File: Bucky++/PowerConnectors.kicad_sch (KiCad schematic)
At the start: 16 parts, among them J1 XT60PW-M, J11 XT30AW-M, J12 XT30AW-M, J13 XT30AW-M, J14 XT30AW-M, J17 XT30UPB-F, J18 XT30UPB-F, J2 XT60PW-F, J3 XT30PW-F, J4 XT30PW-F, J5 XT30PW-F, J6 XT30PW-F, J7 XT30UPB-F, J8 XT30UPB-F

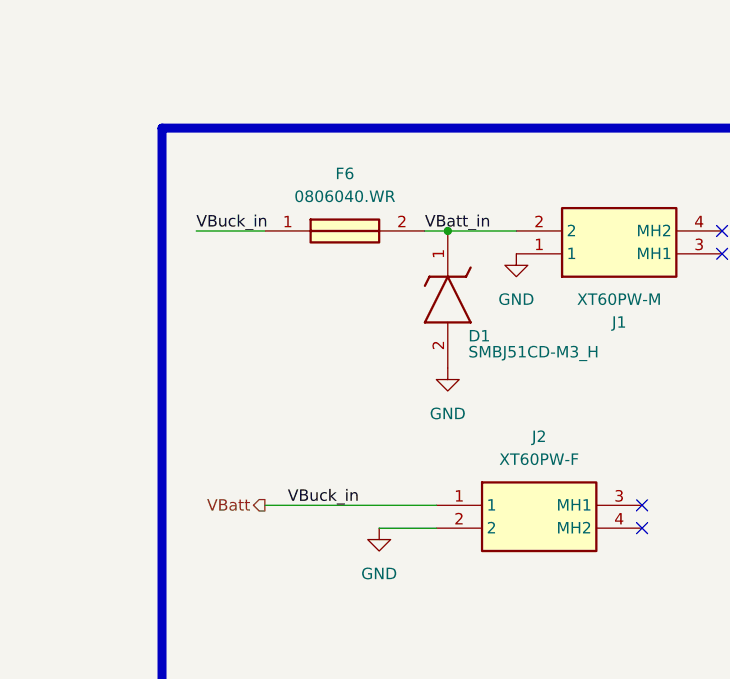
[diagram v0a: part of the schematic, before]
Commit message: added over-current protection on main input
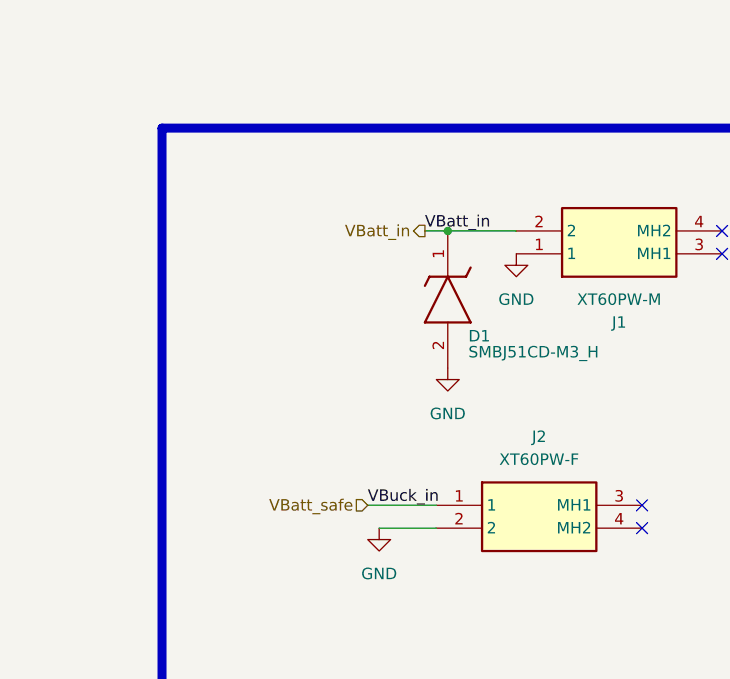
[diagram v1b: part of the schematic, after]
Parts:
- removed F6: 0806040.WR, SamacSys_Parts:FUSC3216X110N, symbol SamacSys_Parts:0806040.WR
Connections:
- net VBatt renamed VBatt_safe
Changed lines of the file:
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@@
 	(wire
 		(pts
-			(xy 36.83 50.8) (xy 44.45 50.8)
+			(xy 55.88 81.28) (xy 63.5 81.28)
 		)
 		(stroke
@@
 		(pts
 			(xy 110.49 92.71) (xy 118.11 92.71)
-		)
-		(stroke
-			(width 0)
-			(type default)
-		)
-	)
-	(wire
-		(pts
-			(xy 44.45 81.28) (xy 63.5 81.28)
 		)
 		(stroke
@@
 	)
 	(label "VBuck_in"
-		(at 36.83 50.8 0)
+		(at 55.88 81.28 0)
 		(effects
 			(font
@@
 	(label "Vout_12V"
 		(at 204.47 135.89 0)
-		(effects
-			(font
-				(size 1.27 1.27)
-			)
-			(justify left bottom)
-		)
-	)
-	(label "VBuck_in"
-		(at 46.99 81.28 0)
 		(effects
 			(font
@@
 		)
 	)
-	(hierarchical_label "VBatt"
+	(hierarchical_label "VBatt_safe"
+		(shape input)
+		(at 55.88 81.28 180)
+		(effects
+			(font
+				(size 1.27 1.27)
+			)
+			(justify right)
+		)
+	)
+	(hierarchical_label "VBatt_in"
 		(shape output)
-		(at 44.45 81.28 180)
+		(at 62.23 50.8 180)
 		(effects
 			(font
@@
 					(unit 1)
 				)
-			)
-		)
-	)
-	(symbol
-		(lib_id "SamacSys_Parts:0806040.WR")
-		(at 44.45 50.8 0)
-		(unit 1)
-		(exclude_from_sim no)
-		(in_bom yes)
-		(on_board yes)
-		(dnp no)
-		(fields_autoplaced yes)
-		(property "Reference" "F6"
-			(at 53.34 44.45 0)
-			(effects
-				(font
-					(size 1.27 1.27)
-				)
-			)
-		)
-		(property "Value" "0806040.WR"
-			(at 53.34 46.99 0)
-			(effects
-				(font
-					(size 1.27 1.27)
-				)
-			)
-		)
-		(property "Footprint" "SamacSys_Parts:FUSC3216X110N"
-			(at 58.42 146.99 0)
-			(effects
-				(font
-					(size 1.27 1.27)
-				)
-				(justify left top)
-				(hide yes)
-			)
-		)
-		(property "Datasheet" "https://www.littelfuse.com/assetdocs/littelfuse-fuse-806-datasheet?assetguid=a8479f54-3b43-4b97-8985-2bc550feee6f"
-			(at 58.42 246.99 0)
-			(effects
-				(font
-					(size 1.27 1.27)
-				)
-				(justify left top)
-				(hide yes)
-			)
-		)
-		(property "Description" "Surface Mount Fuses High Current 40A 36V , FUSE 36V HIGH CURRENT 1206 FA 40A | Series: 806 ,200A @ 36VDC"
-			(at 44.45 50.8 0)
-			(effects
-				(font
-					(size 1.27 1.27)
-				)
-				(hide yes)
-			)
-		)
-		(property "Height" "1.1"
-			(at 58.42 446.99 0)
-			(effects
-				(font
-					(size 1.27 1.27)
-				)
-				(justify left top)
-				(hide yes)
-			)
-		)
-		(property "Mouser Part Number" ""
-			(at 58.42 546.99 0)
-			(effects
-				(font
-					(size 1.27 1.27)
-				)
-				(justify left top)
-				(hide yes)
-			)
-		)
-		(property "Mouser Price/Stock" ""
-			(at 58.42 646.99 0)
-			(effects
-				(font
-					(size 1.27 1.27)
-				)
-				(justify left top)
-				(hide yes)
-			)
-		)
-		(property "Manufacturer_Name" "LITTELFUSE"
-			(at 58.42 746.99 0)
-			(effects
-				(font
-					(size 1.27 1.27)
-				)
-				(justify left top)
-				(hide yes)
-			)
-		)
-		(property "Manufacturer_Part_Number" "0806040.WR"
-			(at 58.42 846.99 0)
-			(effects
-				(font
-					(size 1.27 1.27)
-				)
-				(justify left top)
-				(hide yes)
-			)
-		)
-		(pin "2"
-		)
-		(pin "1"
-		)
-		(instances
-			(project "Bucky++"
-				(path "/0650c7a8-acba-429c-9f8e-eec0baf0bc1c/fede4c36-00cc-4d3d-b71c-5243ba232202/0b884d20-85c8-4e14-bcd5-df65213f1de9"
-					(reference "F6")
-					(unit 1)
-				)

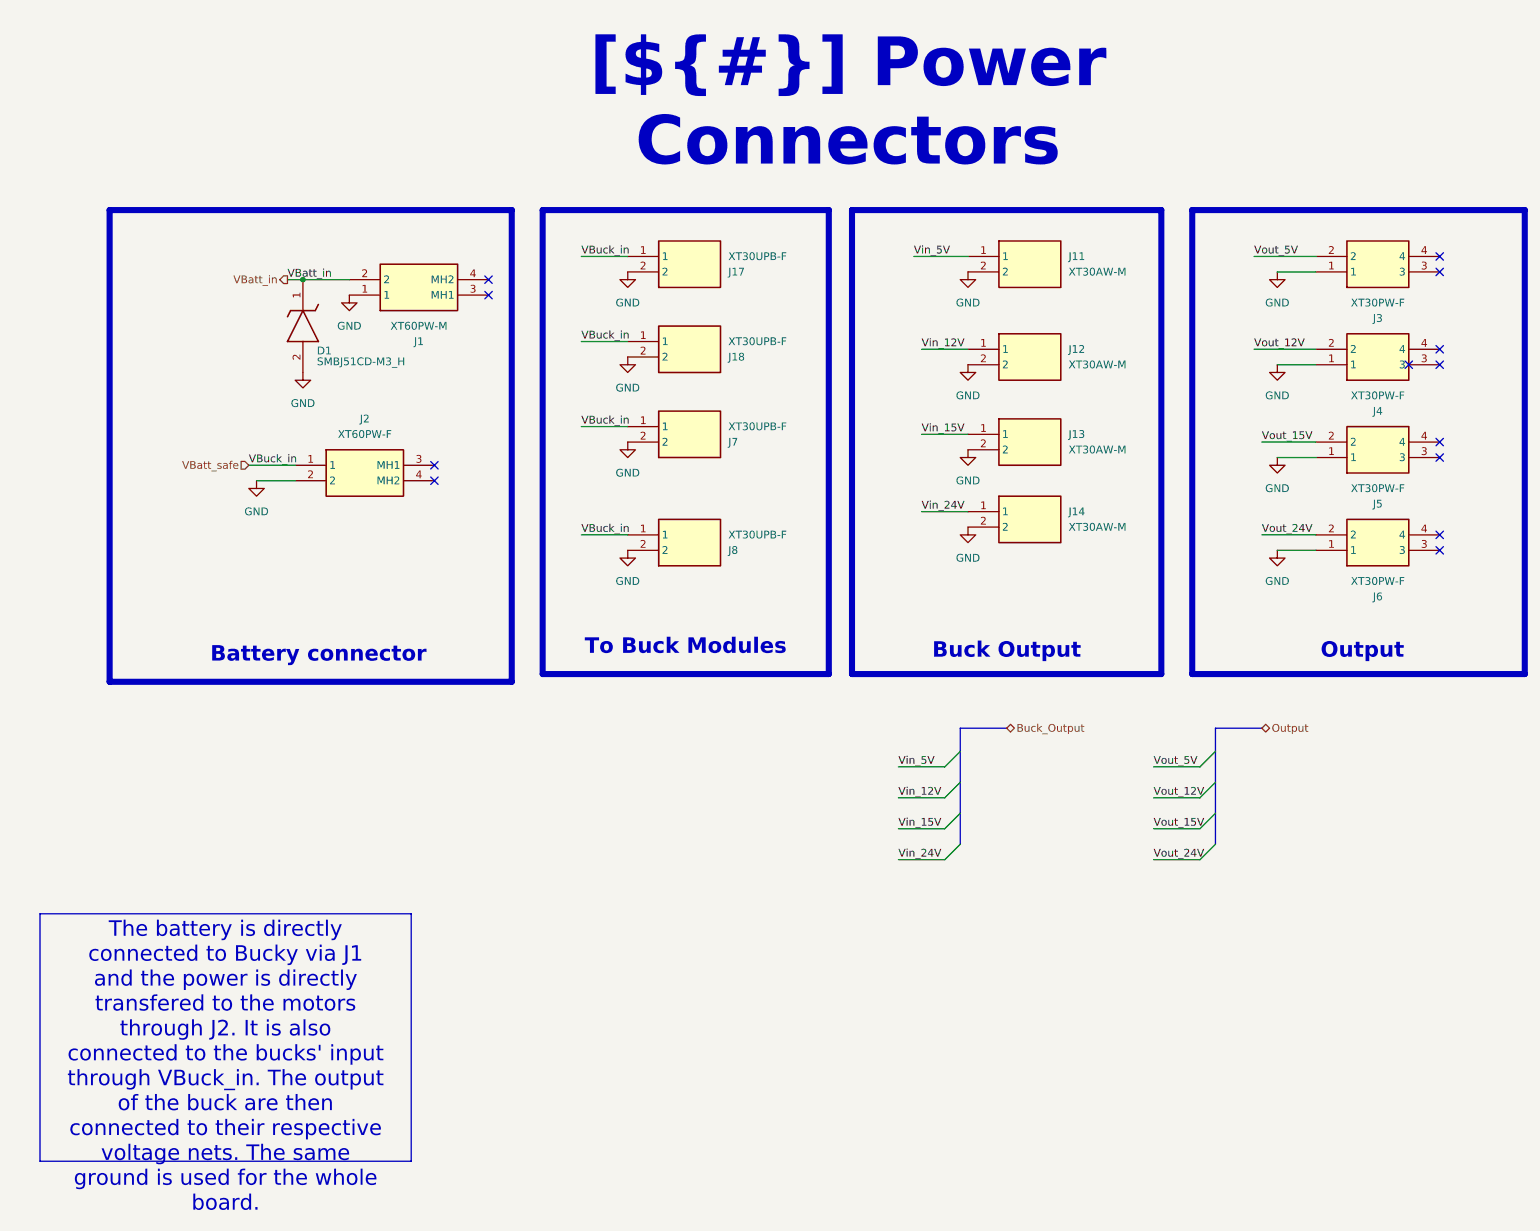
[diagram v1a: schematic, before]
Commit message: fixed errors and added protection diodes
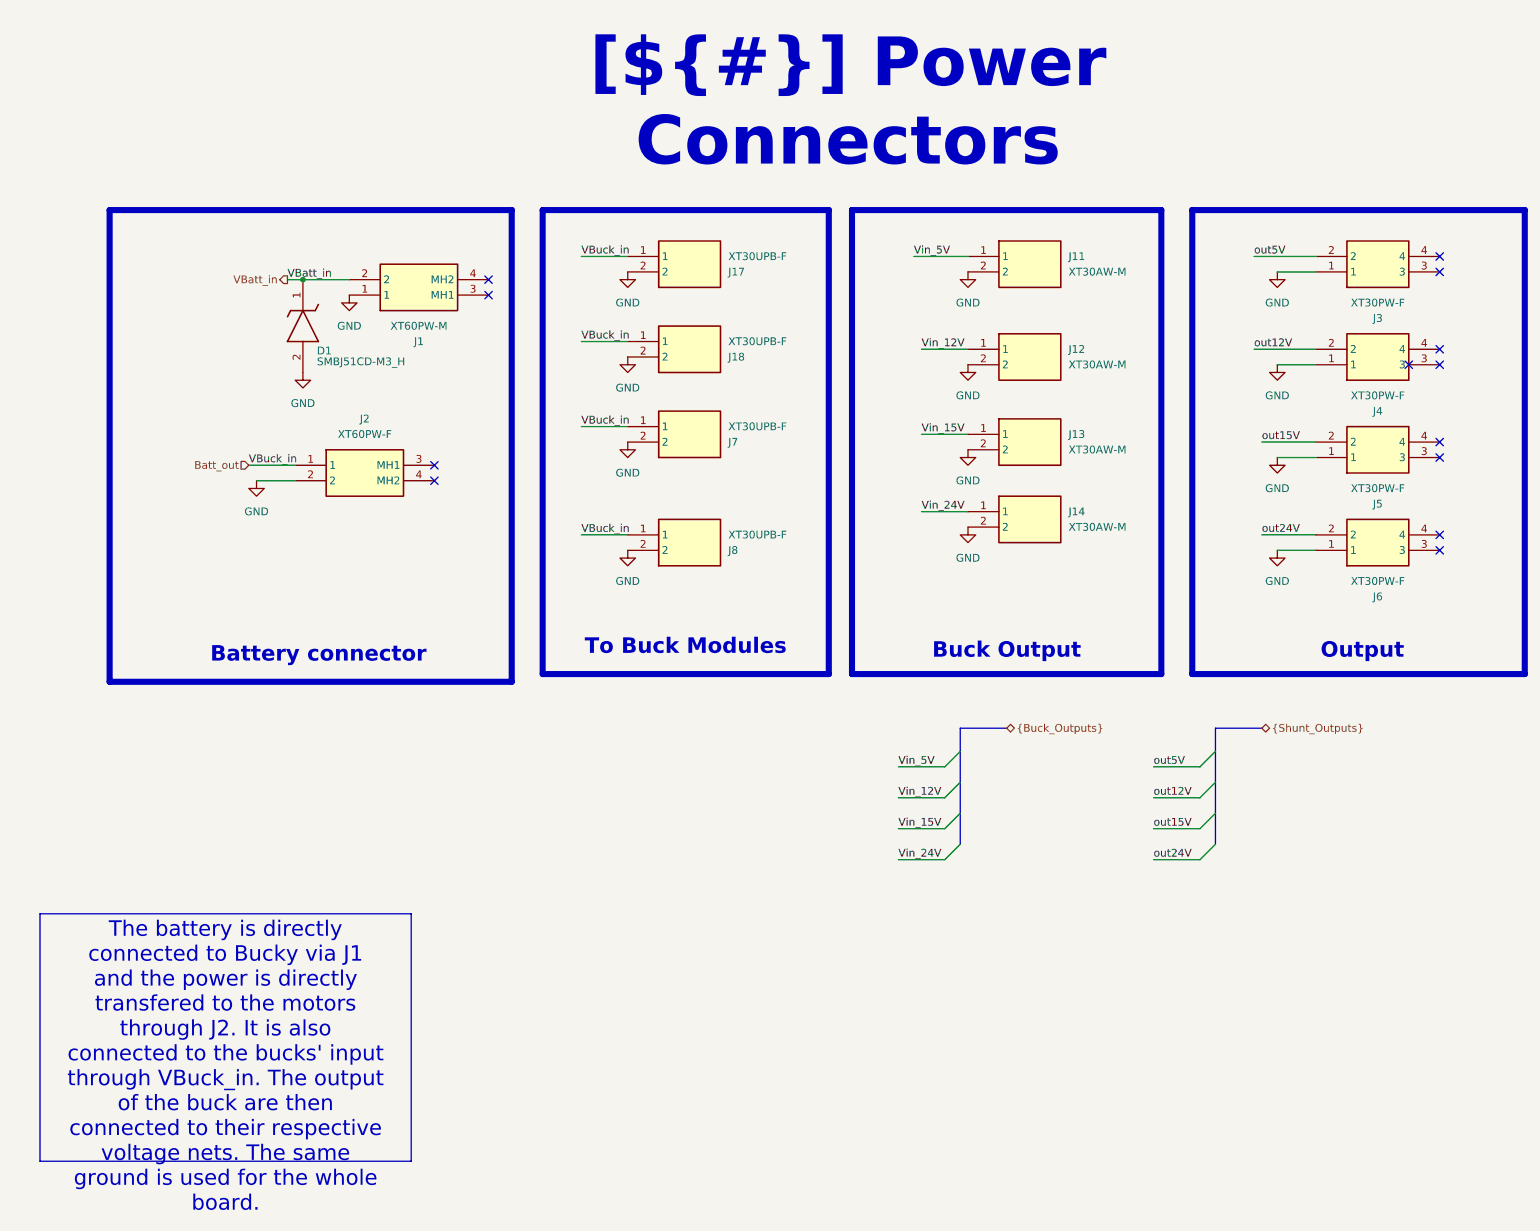
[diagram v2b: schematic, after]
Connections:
- net VBatt_safe renamed Batt_out
- net Vout_12V renamed out12V
- net Vout_15V renamed out15V
- net Vout_24V renamed out24V
- net Vout_5V renamed out5V
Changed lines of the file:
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@@
 		)
 	)
-	(label "Vout_5V"
+	(label "out5V"
 		(at 220.98 46.99 0)
 		(effects
@@
 		)
 	)
-	(label "Vout_24V"
+	(label "out24V"
 		(at 204.47 146.05 0)
 		(effects
@@
 		)
 	)
-	(label "Vout_24V"
+	(label "out24V"
 		(at 222.25 92.71 0)
 		(effects
@@
 		)
 	)
-	(label "Vout_15V"
+	(label "out15V"
 		(at 222.25 77.47 0)
 		(effects
@@
 		)
 	)
-	(label "Vout_12V"
+	(label "out12V"
 		(at 220.98 62.23 0)
 		(effects
@@
 		)
 	)
-	(label "Vout_5V"
+	(label "out5V"
 		(at 204.47 130.81 0)
 		(effects
@@
 		)
 	)
-	(label "Vout_12V"
+	(label "out12V"
 		(at 204.47 135.89 0)
 		(effects
@@
 		)
 	)
-	(label "Vout_15V"
+	(label "out15V"
 		(at 204.47 140.97 0)
 		(effects
@@
 		)
 	)
-	(hierarchical_label "Output"
+	(hierarchical_label "{Shunt_Outputs}"
 		(shape tri_state)
 		(at 222.25 124.46 0)
@@
 		)
 	)
-	(hierarchical_label "VBatt_safe"
+	(hierarchical_label "Batt_out"
 		(shape input)
 		(at 55.88 81.28 180)
@@
 		)
 	)
-	(hierarchical_label "Buck_Output"
+	(hierarchical_label "{Buck_Outputs}"
 		(shape tri_state)
 		(at 180.34 124.46 0)

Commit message: fixed issues after Pedro's review
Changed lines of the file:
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@@
 		)
 	)
-	(text_box "The battery is directly connected to Bucky via J1 and the power is directly transfered to the motors through J2. It is also connected to the bucks' input through VBuck_in. The output of the buck are then connected to their respective voltage nets. The same ground is used for the whole board.\n"
+	(text_box "DESIGN NOTE:\nThe battery is directly connected to Bucky via J1 and the power is directly transfered to the motors through J2. It is also connected to the bucks' input through VBuck_in. \nThe output of the buck are then connected to their respective voltage nets. \nThe same ground is used for the whole board.\n"
 		(exclude_from_sim no)
-		(at 21.59 154.94 0)
-		(size 60.96 40.64)
-		(margins 0.9525 0.9525 0.9525 0.9525)
+		(at 33.02 120.65 0)
+		(size 38.1 27.94)
+		(margins 1.3525 1.3525 1.3525 1.3525)
 		(stroke
-			(width 0.0508)
+			(width 0.8)
 			(type solid)
+			(color 200 200 200 1)
 		)
 		(fill
@@
 			(font
 				(face "Arial")
-				(size 2.54 2.54)
+				(size 1.27 1.27)
+				(bold yes)
 				(color 0 0 0 1)
 			)
-			(justify top)
+			(justify left top)
 		)
 	)
@@
 	)
 	(junction
+		(at 71.12 50.8)
+		(diameter 0)
+		(color 0 0 0 0)
+	)
+	(junction
 		(at 64.77 50.8)
 		(diameter 0)
@@
 	)
 	(bus_entry
-		(at 214.63 138.43)
+		(at 231.14 137.16)
 		(size -2.54 2.54)
 		(stroke
@@
 	)
 	(bus_entry
-		(at 214.63 143.51)
+		(at 231.14 142.24)
 		(size -2.54 2.54)
 		(stroke
@@
 	)
 	(bus_entry
-		(at 172.72 143.51)
+		(at 179.07 142.24)
 		(size -2.54 2.54)
 		(stroke
@@
 	)
 	(bus_entry
-		(at 214.63 128.27)
+		(at 231.14 127)
 		(size -2.54 2.54)
 		(stroke
@@
 	)
 	(bus_entry
-		(at 172.72 133.35)
+		(at 179.07 132.08)
 		(size -2.54 2.54)
 		(stroke
@@
 	)
 	(bus_entry
-		(at 214.63 133.35)
+		(at 231.14 132.08)
 		(size -2.54 2.54)
 		(stroke
@@
 	)
 	(bus_entry
-		(at 172.72 138.43)
+		(at 179.07 137.16)
 		(size -2.54 2.54)
 		(stroke
@@
 	)
 	(bus_entry
-		(at 172.72 128.27)
+		(at 179.07 127)
 		(size -2.54 2.54)
 		(stroke
@@
 	(bus
 		(pts
-			(xy 214.63 128.27) (xy 214.63 124.46)
+			(xy 231.14 127) (xy 231.14 123.19)
 		)
 		(stroke
@@
 	(wire
 		(pts
-			(xy 64.77 50.8) (xy 72.39 50.8)
+			(xy 64.77 50.8) (xy 71.12 50.8)
 		)
 		(stroke
@@
 	(bus
 		(pts
-			(xy 214.63 143.51) (xy 214.63 138.43)
+			(xy 231.14 142.24) (xy 231.14 137.16)
 		)
 		(stroke
@@
 	(wire
 		(pts
-			(xy 204.47 135.89) (xy 212.09 135.89)
+			(xy 220.98 134.62) (xy 228.6 134.62)
 		)
 		(stroke
@@
 	(bus
 		(pts
-			(xy 172.72 133.35) (xy 172.72 128.27)
+			(xy 179.07 132.08) (xy 179.07 127)
 		)
 		(stroke
@@
 	(wire
 		(pts
-			(xy 204.47 130.81) (xy 212.09 130.81)
+			(xy 220.98 129.54) (xy 228.6 129.54)
 		)
 		(stroke
@@
 	(bus
 		(pts
-			(xy 214.63 124.46) (xy 222.25 124.46)
+			(xy 231.14 123.19) (xy 238.76 123.19)
 		)
 		(stroke
@@
 	(bus
 		(pts
-			(xy 172.72 138.43) (xy 172.72 133.35)
+			(xy 179.07 137.16) (xy 179.07 132.08)
 		)
 		(stroke
@@
 	(bus
 		(pts
-			(xy 172.72 124.46) (xy 180.34 124.46)
+			(xy 179.07 123.19) (xy 186.69 123.19)
 		)
 		(stroke
@@
 	(wire
 		(pts
-			(xy 162.56 146.05) (xy 170.18 146.05)
+			(xy 168.91 144.78) (xy 176.53 144.78)
+		)
+		(stroke
+			(width 0)
+			(type default)
+		)
+	)
+	(wire
+		(pts
+			(xy 71.12 50.8) (xy 72.39 50.8)
 		)
 		(stroke
@@
 	(bus
 		(pts
-			(xy 214.63 138.43) (xy 214.63 133.35)
+			(xy 231.14 137.16) (xy 231.14 132.08)
 		)
 		(stroke
@@
 	(wire
 		(pts
-			(xy 162.56 130.81) (xy 170.18 130.81)
+			(xy 168.91 129.54) (xy 176.53 129.54)
 		)
 		(stroke
@@
 	(wire
 		(pts
-			(xy 162.56 135.89) (xy 170.18 135.89)
+			(xy 168.91 134.62) (xy 176.53 134.62)
 		)
 		(stroke
@@
 	(bus
 		(pts
-			(xy 214.63 133.35) (xy 214.63 128.27)
+			(xy 231.14 132.08) (xy 231.14 127)
 		)
 		(stroke
@@
 	(wire
 		(pts
-			(xy 204.47 146.05) (xy 212.09 146.05)
+			(xy 220.98 144.78) (xy 228.6 144.78)
 		)
 		(stroke
@@
 	(bus
 		(pts
-			(xy 172.72 143.51) (xy 172.72 138.43)
+			(xy 179.07 142.24) (xy 179.07 137.16)
 		)
 		(stroke
@@
 	(wire
 		(pts
-			(xy 204.47 140.97) (xy 212.09 140.97)
+			(xy 220.98 139.7) (xy 228.6 139.7)
 		)
 		(stroke
@@
 	(wire
 		(pts
-			(xy 162.56 140.97) (xy 170.18 140.97)
+			(xy 168.91 139.7) (xy 176.53 139.7)
 		)
 		(stroke
@@
 	(bus
 		(pts
-			(xy 172.72 128.27) (xy 172.72 124.46)
+			(xy 179.07 127) (xy 179.07 123.19)
 		)
 		(stroke
@@
 	)
 	(label "Vin_5V"
-		(at 162.56 130.81 0)
+		(at 168.91 129.54 0)
 		(effects
 			(font
@@
 	)
 	(label "out24V"
-		(at 204.47 146.05 0)
+		(at 220.98 144.78 0)
 		(effects
 			(font
@@
 	)
 	(label "Vin_15V"
-		(at 162.56 140.97 0)
+		(at 168.91 139.7 0)
 		(effects
 			(font
@@
 	)
 	(label "Vin_24V"
-		(at 162.56 146.05 0)
+		(at 168.91 144.78 0)
 		(effects
 			(font
@@
 	)
 	(label "Vin_12V"
-		(at 162.56 135.89 0)
+		(at 168.91 134.62 0)
 		(effects
 			(font
@@
 	)
 	(label "out5V"
-		(at 204.47 130.81 0)
+		(at 220.98 129.54 0)
 		(effects
 			(font
@@
 	)
 	(label "out12V"
-		(at 204.47 135.89 0)
+		(at 220.98 134.62 0)
 		(effects
 			(font
@@
 	)
 	(label "out15V"
-		(at 204.47 140.97 0)
+		(at 220.98 139.7 0)
 		(effects
 			(font
@@
 	(hierarchical_label "{Shunt_Outputs}"
 		(shape tri_state)
-		(at 222.25 124.46 0)
+		(at 238.76 123.19 0)
 		(effects
 			(font
@@
 	(hierarchical_label "{Buck_Outputs}"
 		(shape tri_state)
-		(at 180.34 124.46 0)
+		(at 186.69 123.19 0)
 		(effects
 			(font
@@
 					(unit 1)
 				)
+			)
+		)
+	)
+	(symbol
+		(lib_id "power:PWR_FLAG")
+		(at 71.12 50.8 0)
+		(unit 1)
+		(exclude_from_sim no)
+		(in_bom yes)
+		(on_board yes)
+		(dnp no)
+		(fields_autoplaced yes)
+		(property "Reference" "#FLG07"
+			(at 71.12 48.895 0)
+			(effects
+				(font
+					(size 1.27 1.27)
+				)
+				(hide yes)
+			)
+		)
+		(property "Value" "PWR_FLAG"
+			(at 71.12 45.72 0)
+			(effects
+				(font
+					(size 1.27 1.27)
+				)
+			)
+		)
+		(property "Footprint" ""
+			(at 71.12 50.8 0)
+			(effects
+				(font
+					(size 1.27 1.27)
+				)
+				(hide yes)
+			)
+		)
+		(property "Datasheet" "~"
+			(at 71.12 50.8 0)
+			(effects
+				(font
+					(size 1.27 1.27)
+				)
+				(hide yes)
+			)
+		)
+		(property "Description" "Special symbol for telling ERC where power comes from"
+			(at 71.12 50.8 0)
+			(effects
+				(font
+					(size 1.27 1.27)
+				)
+				(hide yes)
+			)
+		)
+		(pin "1"
+		)
+		(instances
+			(project "Bucky++"
+				(path "/0650c7a8-acba-429c-9f8e-eec0baf0bc1c/fede4c36-00cc-4d3d-b71c-5243ba232202/0b884d20-85c8-4e14-bcd5-df65213f1de9"
+					(reference "#FLG07")
+					(unit 1)
+				)
